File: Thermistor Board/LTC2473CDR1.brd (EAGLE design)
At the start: 25.4 x 30.4 mm, 31 parts, among them J1 282834-4, J2 I2C, J3 I2C in, J4 I2C out, U1 LTC2473IMS#PBF, U2 LTC2473IMS#PBF

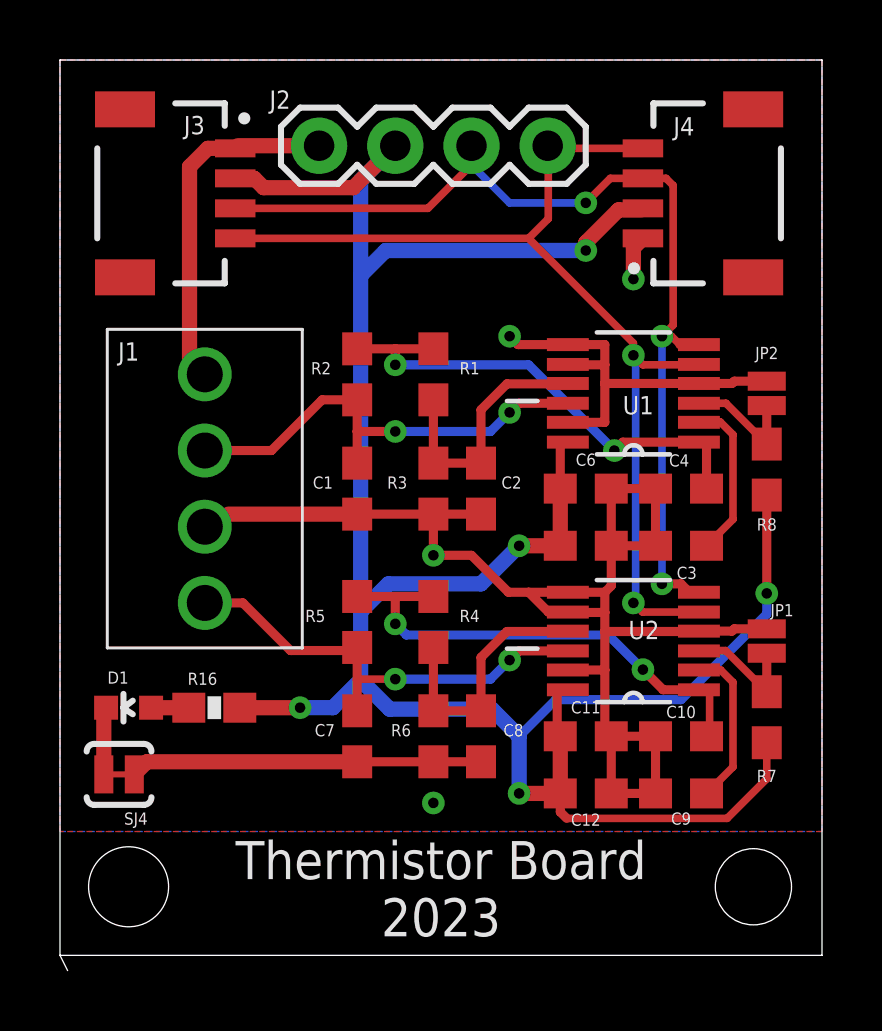
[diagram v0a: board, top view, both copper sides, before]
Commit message: Thermistor Board
Thermistor board with BOM and GERBER files for manufacturing and assembly
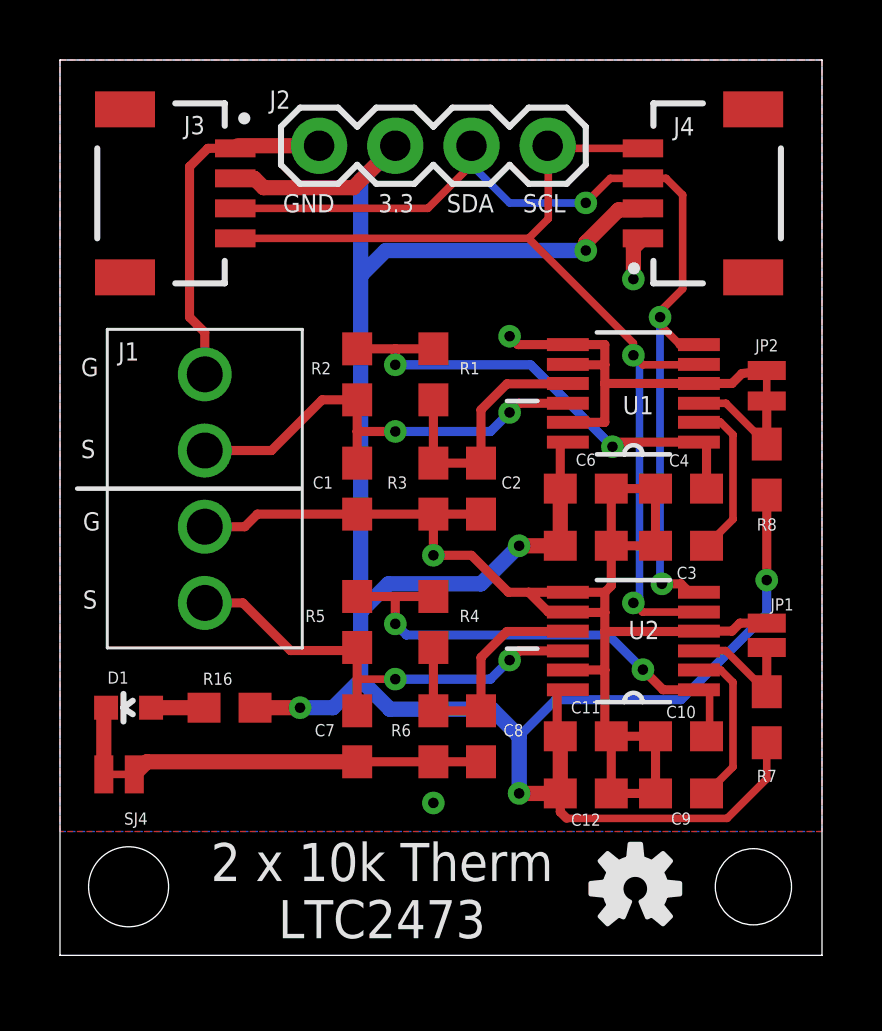
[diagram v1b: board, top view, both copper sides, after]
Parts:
- added FRAME1: FRAME-LETTERNO_PACKAGE, SparkFun-Aesthetics:DUMMY
- added U$1: (no value), SparkFun-Aesthetics:OSHW-LOGO-S
- J3: value I2C in -> I2C
- J4: value I2C out -> I2C
- JP2: value JUMPER-SMT_2_NO_NO-SILK -> JUMPER-SMT_2_NC_TRACE_NO-SILK; device SparkFun-Jumpers:SMT-JUMPER_2_NO_NO-SILK -> SparkFun-Jumpers:SMT-JUMPER_2_NC_TRACE_NO-SILK
- R1, R2, R3, R4, R5, R6: value 0.1 -> 10k
- R16: device SparkFun-Resistors:0603-RES -> SparkFun-Resistors:0603
- SJ4: device SparkFun-Passives:SJ_2S-TRACE -> SparkFun-Jumpers:SMT-JUMPER_2_NC_TRACE_NO-SILK
- moved R16 0.51 mm to (5.65, 8.26)
- moved JP2 0.25 mm to (23.6, 19.0)
- moved JP1 0.19 mm to (23.6, 10.7)
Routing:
- net SDA: track 33.7 -> 34.5 mm
- net 3.3V: track 87.0 -> 86.5 mm
- net N$6: track 1.26 -> 1.77 mm
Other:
- board size 25.4 x 30.4 mm -> 25.4 x 29.8 mm
- board text added: "2 x 10k Therm LTC2473"
- board text added: "3.3"
- board text added: "G"
- board text added: "GND"
- board text added: "S"
- board text added: "SCL"
- board text added: "SDA"
- board text removed: "Thermistor Board 2023"
